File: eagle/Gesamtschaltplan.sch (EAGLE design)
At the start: 176 parts, among them IC1 ATMEGA328P, IC2 LM350T, IC3 LM350T, IC4 7818TV, IC5 DCDC-WANDLER, Q1 AUIRF8409, Q10 AUIRF8409, Q11 AUIRF8409, Q12 AUIRF8409, Q13 AUIRF8409, Q14 AUIRF8409, Q15 AUIRF8409, Q16 AUIRF8409, Q17 AUIRF8409, Q18 AUIRF8409, Q19 AUIRF8409, Q2 AUIRF8409, Q20 AUIRF8409, Q21 BC550C, Q3 AUIRF8409, Q4 IRF1234, Q5 IRF1234, Q6 IRF1234, Q7 IRF1234, Q8 IRF1234, Q9 IRF1234, X1 MKDSN1,5/2-5,08, X2 MKDSN1,5/2-5,08, X3 MKDSN1,5/2-5,08, X4 MKDSN1,5/2-5,08, X5 MKDSN1,5/2-5,08, X6 MKDSN1,5/3-5,08, X7 1751251

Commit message: Minor documentation changes, reduced size of vsens Resistor to detect contact
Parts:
- added S6: (no value), switch:255SB
- R58: value 2k -> 150k
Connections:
- removed net N$78: C5.+, D13.C, D4.C, D8.A, Q1.D, Q16.D, Q17.D, Q18.D, Q19.D, Q2.D, Q3.D
- new net N$15: C4.+, D12.C, D5.C, D9.A, Q4.D, Q5.D, Q6.D, Q7.D, Q8.D, Q9.D
- new net N$21: D4.A, D6.A, R12.1, R13.1, R14.1, R15.1, R16.1
- net C1V: now also C5.+, D13.C, D4.C, D8.A, Q1.D, Q16.D, Q17.D, Q18.D, Q19.D, Q2.D, Q3.D; no longer D4.A, D6.A, R12.1, R13.1, R14.1, R15.1, R16.1
- net C2V: no longer C4.+, D12.C, D5.C, D9.A, Q4.D, Q5.D, Q6.D, Q7.D, Q8.D, Q9.D
- net GND: now also S6.P
- net N$12: now also S6.S
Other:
- moved on the sheet: F1, F2, S1, X7-1, X7-2, X7-3

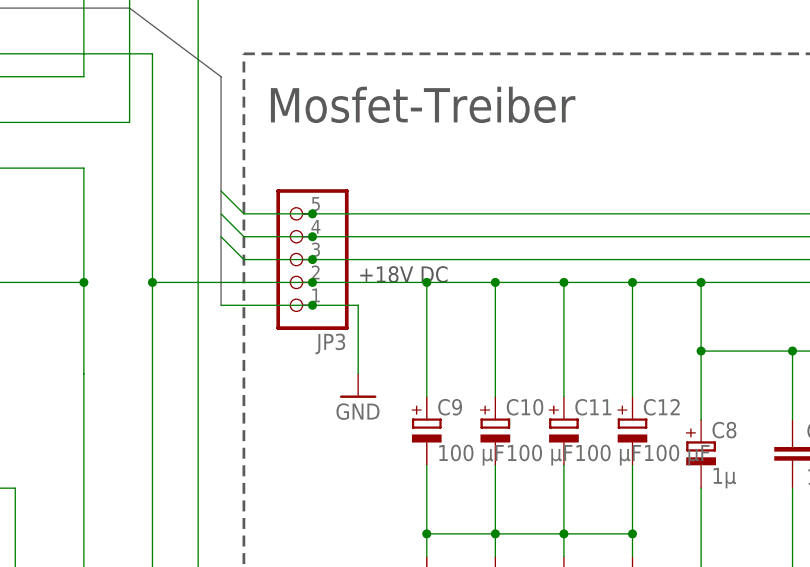
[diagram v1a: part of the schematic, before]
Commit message: additional diode at Mosfet driver
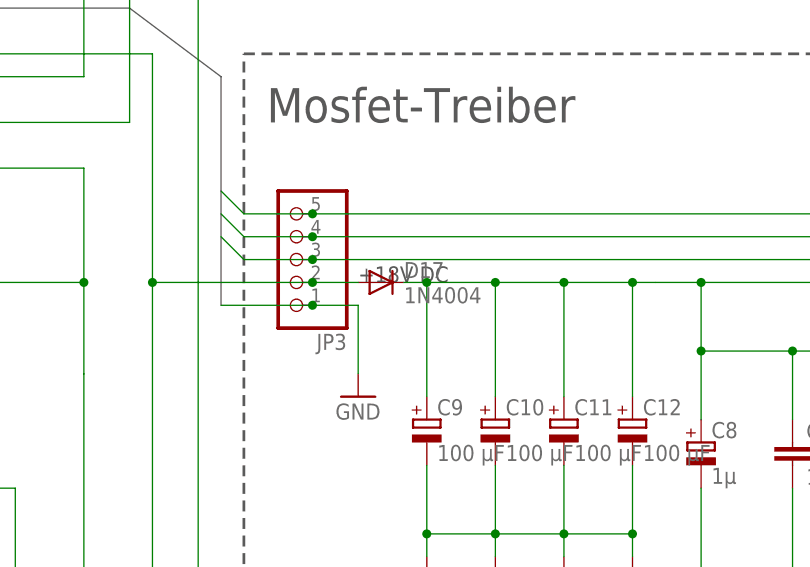
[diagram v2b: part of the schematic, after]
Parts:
- added D17: 1N4004, diode:1N4004
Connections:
- new net N$31: C10.+, C11.+, C12.+, C13.+, C21.1, C22.1, C24.1, C7.+, C8.+, C9.+, D17.C, U$4.VDD, U$5.VDD, U$6.VDD
- net N$3: now also D17.A; no longer C10.+, C11.+, C12.+, C13.+, C21.1, C22.1, C24.1, C7.+, C8.+, C9.+, U$4.VDD, U$5.VDD, U$6.VDD
